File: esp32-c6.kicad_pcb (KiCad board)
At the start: 2 copper layers, 97.1 x 66.5 mm, 80 parts, among them J1 USB_C_Receptacle_USB2.0_14P, J2 USB_C_Receptacle_USB2.0_14P, J3 54-00166, J4 Conn_01x08_Socket, J5 Conn_01x06_Socket, J6 Conn_01x04, J7 Conn_01x10_Socket, J8 Conn_01x08_Socket, J9 Conn_02x03_Counter_Clockwise, Q1 BC847BDW1, SW1 SW_Push, SW2 SW_Push, U1 CP2102N-Axx-xQFN28, U2 MPQ9841GLE-5-AEC1-Z, U3 NCP1117-3.3_SOT223, U4 ESP32-C6-WROOM-1-N8

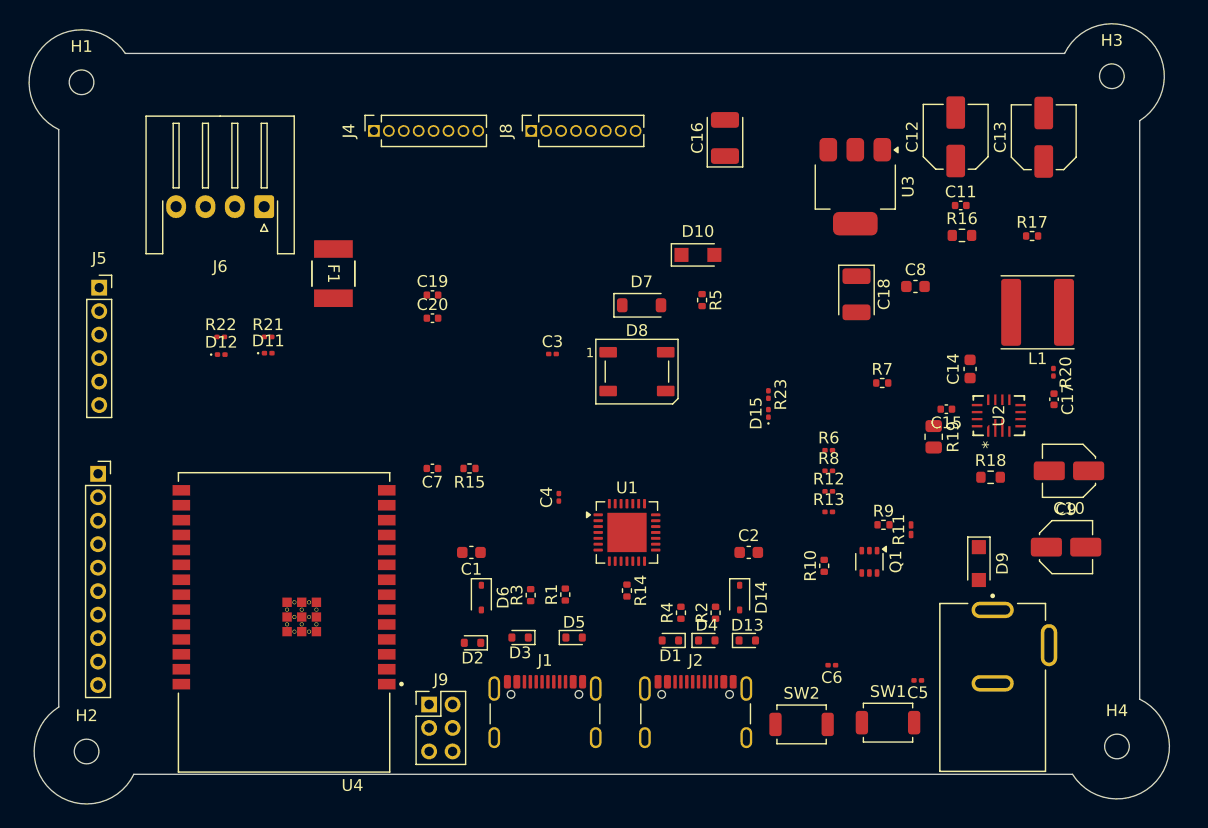
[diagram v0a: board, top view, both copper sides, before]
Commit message: layout + power pin traces
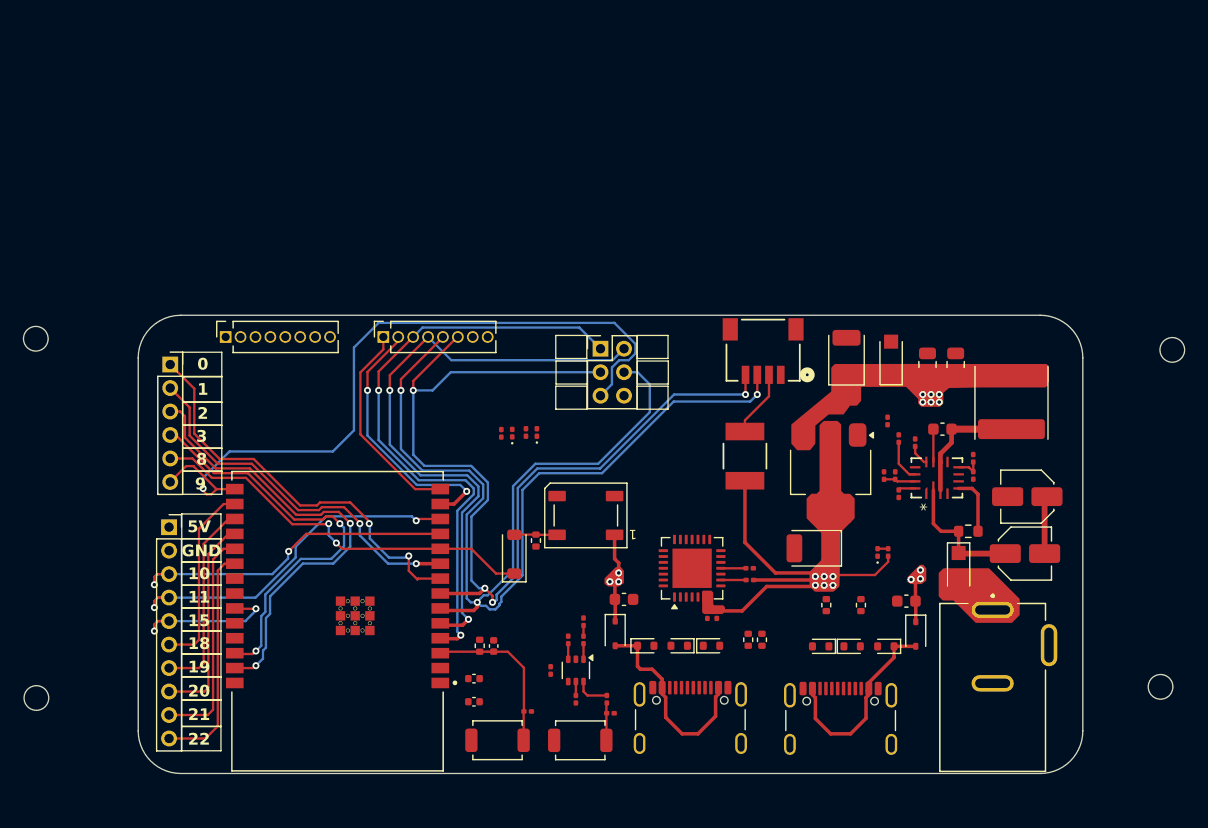
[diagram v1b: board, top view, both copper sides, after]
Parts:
- removed R6: 0, Resistor_SMD:R_0201_0603Metric
- C11, C15, C17: footprint Capacitor_SMD:C_0402_1005Metric -> Capacitor_SMD:C_0201_0603Metric
- C12, C13: footprint Capacitor_SMD:C_Elec_5x5.8 -> Capacitor_SMD:C_0805_2012Metric
- C14: footprint Capacitor_SMD:C_0603_1608Metric -> Capacitor_SMD:C_0201_0603Metric
- J6: footprint Connector_JST:JST_XH_S4B-XH-A-1_1x04_P2.50mm_Horizontal -> uno-esp:CONN_SM04B-SRSS-TB_JST
- R10, R14, R17, R7, R9: footprint Resistor_SMD:R_0402_1005Metric -> Resistor_SMD:R_0201_0603Metric
- R11: footprint Resistor_SMD:R_0201_0603Metric_Pad0.64x0.40mm_HandSolder -> Resistor_SMD:R_0201_0603Metric
- R16: footprint Resistor_SMD:R_0603_1608Metric -> Resistor_SMD:R_0201_0603Metric
- R19: footprint Resistor_SMD:R_0805_2012Metric -> Resistor_SMD:R_0201_0603Metric
- moved J6 44.2 mm to (222.2, 146.5), turned to 0 degrees
- moved F1 38.3 mm to (220.7, 155.6)
- moved J9 33.6 mm to (208.3, 146.4)
- moved C19 32.9 mm to (197.6, 174.5)
- moved C20 32.9 mm to (197.6, 176.5)
- moved R11 29.0 mm to (206.9, 169.7), turned to -90 degrees
- moved R12 27.9 mm to (206.2, 176.3), turned to -90 degrees
- moved D12 27.7 mm to (202.9, 153.5), turned to 90 degrees
- moved R9 27.4 mm to (206.9, 171.2), turned to 90 degrees
- moved R22 27.2 mm to (202.0, 153.5), turned to 90 degrees
- moved R8 27.1 mm to (208.9, 176.3), turned to 90 degrees
- moved Q1 26.7 mm to (206.2, 173.8)
- moved C5 26.3 mm to (209.2, 177.4)
- moved SW1 26.3 mm to (206.6, 179.8)
- moved C3 26.2 mm to (218.2, 169.1), turned to -90 degrees
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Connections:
- C6 pad 2: /EN -> EN
- C7 pad 1: /EN -> EN
- D7 pad 1: /GPIO8 -> IO8
- D8 pad 4: Net-(D8-DIN) -> Net-(D7-A)
- J4 pad 3: /esp32-c6 Pinout/EN -> EN
- J5 pad 5: /esp32-c6 Pinout/IO8 -> IO8
- J9 pad 3: /esp32-c6 Pinout/IO7_TD0 -> /esp32-c6 Pinout/IO7_SCL
- J9 pad 4: /esp32-c6 Pinout/IO6_TCK -> /esp32-c6 Pinout/IO6_SDA
- R15 pad 2: /EN -> EN
- SW2 pad 2: /EN -> EN
- U1 pad 4: /D+_A -> /DA_P
- U1 pad 5: /D-_A -> /DA_N
- U4 pad 10: /esp32-c6 Pinout/IO8 -> IO8
- U4 pad 3: /esp32-c6 Pinout/EN -> EN
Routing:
- net /esp32-c6 Pinout/IO6_SDA: track 0.00 -> 103.0 mm, vias 0 -> 3
- net /esp32-c6 Pinout/IO7_SCL: track 0.00 -> 86.5 mm, vias 0 -> 4
- net /esp32-c6 Pinout/IO9_BOOT: track 0.00 -> 62.7 mm, vias 0 -> 1
- net /esp32-c6 Pinout/IO5_TDI: track 0.00 -> 52.3 mm, vias 0 -> 2
- net /esp32-c6 Pinout/IO4_TMS: track 0.00 -> 52.1 mm, vias 0 -> 2
- net /esp32-c6 Pinout/IO2: track 0.00 -> 39.5 mm, vias 0 -> 2
- net /esp32-c6 Pinout/IO3: track 0.00 -> 35.3 mm, vias 0 -> 2
- net +3.3V: track 0.00 -> 35.1 mm, vias 0 -> 6
- net /esp32-c6 Pinout/IO0: track 0.00 -> 34.7 mm, vias 0 -> 2
- net IO8: track 0.00 -> 34.0 mm, vias 0 -> 2
- net /esp32-c6 Pinout/IO1: track 0.00 -> 31.4 mm, vias 0 -> 2
- net /esp32-c6 Pinout/IO11: track 0.00 -> 30.8 mm, vias 0 -> 2
- net /esp32-c6 Pinout/IO10: track 0.00 -> 28.8 mm, vias 0 -> 2
- net /esp32-c6 Pinout/IO12_DB_N: track 0.00 -> 22.6 mm, vias 0 -> 2
- net /esp32-c6 Pinout/IO22: track 0.00 -> 19.5 mm
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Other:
- board size 97.1 x 66.5 mm -> 80.5 x 39 mm
- copper layers 2 -> 4
- board text added: "0"
- board text added: "1"
- board text added: "10"
- board text added: "11"
- board text added: "15"
- board text added: "18"
- board text added: "19"
- board text added: "2"
- board text added: "20"
- board text added: "21"
- board text added: "22"
- board text added: "3"
- board text added: "5V"
- board text added: "8"
- board text added: "9"
- board text added: "GND"

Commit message: final tracing + pcb layers + colors
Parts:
- removed H1, H2, H3, H4: MountingHole, MountingHole:MountingHole_2.1mm
- removed J9: Conn_02x03_Counter_Clockwise, Connector_PinHeader_2.00mm:PinHeader_2x03_P2.00mm_Vertical
- added R6: 0, Resistor_SMD:R_0402_1005Metric_Pad0.72x0.64mm_HandSolder, F.Cu at (181.8, 152.7)
- J4: footprint Connector_PinSocket_1.27mm:PinSocket_1x08_P1.27mm_Vertical -> Connector_PinSocket_2.00mm:PinSocket_1x08_P2.00mm_Vertical
- J8: value Conn_01x08_Socket -> Conn_01x06_Socket; footprint Connector_PinSocket_1.27mm:PinSocket_1x08_P1.27mm_Vertical -> Connector_PinSocket_2.00mm:PinSocket_1x06_P2.00mm_Vertical
- moved J6 28.0 mm to (194.2, 146.5)
- moved J4 24.7 mm to (201.1, 145.4)
- moved F1 23.9 mm to (196.8, 153.4), turned to 0 degrees
- moved D11 20.8 mm to (180.1, 152.4), turned to -90 degrees
- moved R21 20.3 mm to (179.8, 150.9), turned to 180 degrees
- moved D12 19.5 mm to (183.5, 152.4), turned to -90 degrees
- moved R22 19.0 mm to (183.2, 151.0), turned to 180 degrees
- moved D10 13.8 mm to (219.3, 146.1), turned to 180 degrees
- moved J8 12.6 mm to (177.2, 145.4)
- moved D1 2.68 mm to (229.8, 171.8), turned to 0 degrees
- moved D4 2.68 mm to (227.1, 171.8), turned to 180 degrees
- moved C20 2.43 mm to (197.1, 174.1), turned to -90 degrees
- moved C19 0.66 mm to (198.1, 174.1), turned to -90 degrees
- turned D7 to -90 degrees
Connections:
- C9 pad 1: /Barrel Jack/VIN -> VIN
- D1 pad 1: /IO13_DB_P -> DB_P
- D10 pad 1: +5V -> VIN
- D10 pad 2: VBUS -> Net-(D10-A)
- D4 pad 1: /IO12_DB_N -> DB_N
- D9 pad 1: /Barrel Jack/VIN -> VIN
- D9 pad 2: V_IN -> VIN
- J2 pad A6: /IO13_DB_P -> DB_P
- J2 pad A7: /IO12_DB_N -> DB_N
- J2 pad B6: /IO13_DB_P -> DB_P
- J2 pad B7: /IO12_DB_N -> DB_N
- J3 pad A: V_IN -> VIN
- J4 pad 8: VIN -> Net-(D10-A)
- J8 pad 1: /esp32-c6 Pinout/IO13_DB_P -> /esp32-c6 Pinout/IO4_TMS
- J8 pad 2: /esp32-c6 Pinout/IO12_DB_N -> /esp32-c6 Pinout/IO5_TDI
- J8 pad 3: /esp32-c6 Pinout/IO4_TMS -> /esp32-c6 Pinout/IO6_SDA
- J8 pad 4: /esp32-c6 Pinout/IO5_TDI -> /esp32-c6 Pinout/IO7_SCL
- J8 pad 5: /esp32-c6 Pinout/IO6_SDA -> /esp32-c6 Pinout/UART_TX
- J8 pad 6: /esp32-c6 Pinout/IO7_SCL -> /esp32-c6 Pinout/UART_RX
- R18 pad 1: /Barrel Jack/VIN -> VIN
- U2 pad 2: /Barrel Jack/VIN -> VIN
- U4 pad 13: /esp32-c6 Pinout/IO12_DB_N -> DB_N
- U4 pad 14: /esp32-c6 Pinout/IO13_DB_P -> DB_P
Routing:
- net +5V: track 11.4 -> 134.3 mm, vias 12 -> 14
- net +3.3V: track 35.1 -> 144.4 mm, vias 6 -> 9
- net /esp32-c6 Pinout/IO9_BOOT: track 62.7 -> 6.87 mm, vias 1 -> 0
- net VIN: track 0.00 -> 50.3 mm, vias 0 -> 4
- net DB_P: track 0.00 -> 49.8 mm, vias 0 -> 2
- net DB_N: track 0.00 -> 47.5 mm, vias 0 -> 2
- net EN: track 13.9 -> 48.8 mm, vias 0 -> 1
- net /esp32-c6 Pinout/UART_RX: track 0.00 -> 32.2 mm, vias 0 -> 2
- net /esp32-c6 Pinout/UART_TX: track 0.00 -> 31.8 mm, vias 0 -> 2
- net /esp32-c6 Pinout/IO6_SDA: track 103.0 -> 72.9 mm, vias 3 -> 1
- net /esp32-c6 Pinout/IO12_DB_N: track 22.6 -> 0.00 mm, vias 2 -> 0
- net /esp32-c6 Pinout/IO13_DB_P: track 17.8 -> 0.00 mm
- net /esp32-c6 Pinout/IO7_SCL: track 86.5 -> 69.5 mm, vias 4 -> 1
- net /DA_N: track 0.00 -> 12.9 mm, vias 0 -> 1
- net Net-(J2-CC2): track 0.00 -> 12.6 mm, vias 0 -> 2
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- added copper zone on B.Cu, net GND
- added copper zone on F.Cu, net GND
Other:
- board size 80.5 x 39 mm -> 78.5 x 39 mm
- copper layers 4 -> 2
- board text added: "3.3"
- board text added: "4"
- board text added: "5"
- board text added: "6"
- board text added: "7"
- board text added: "EN"
- board text added: "RX"
- board text added: "TX"
- board text added: "VIN"

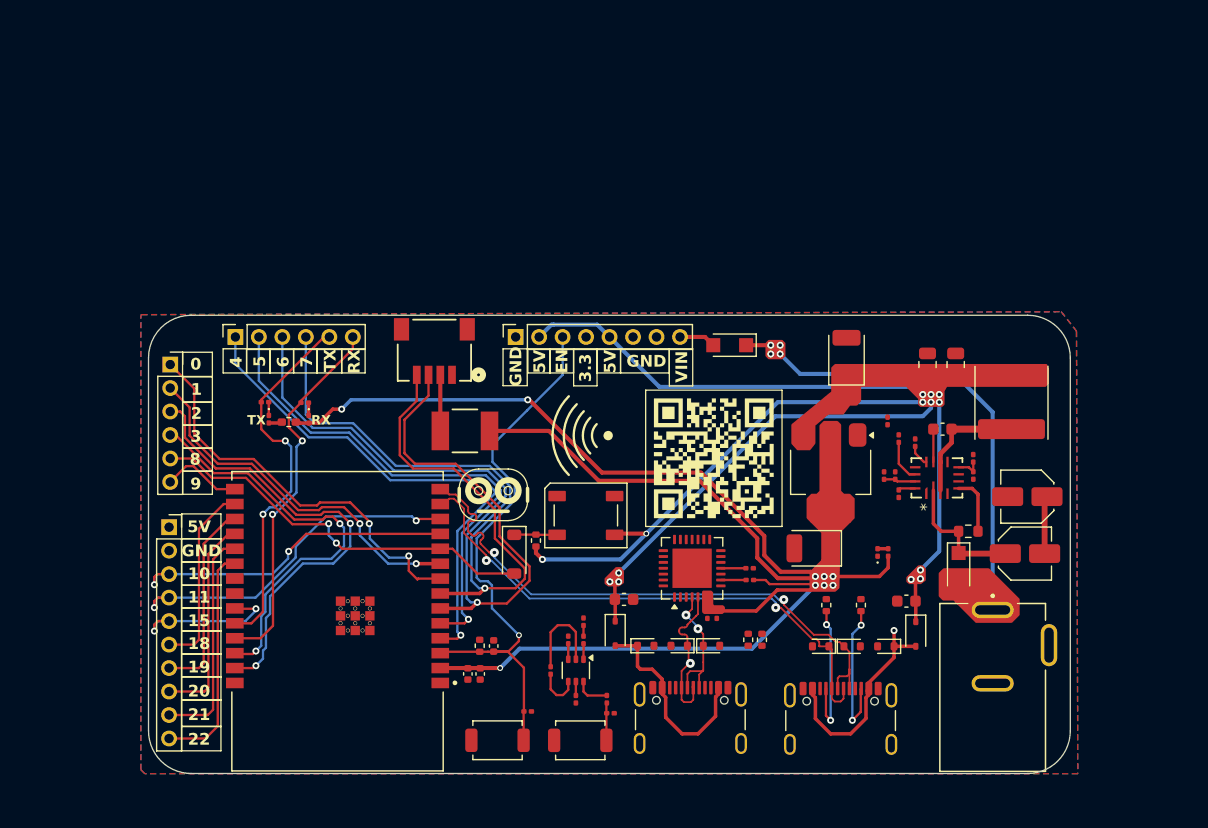
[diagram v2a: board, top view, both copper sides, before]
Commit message: minor silkscreen changes + readme file
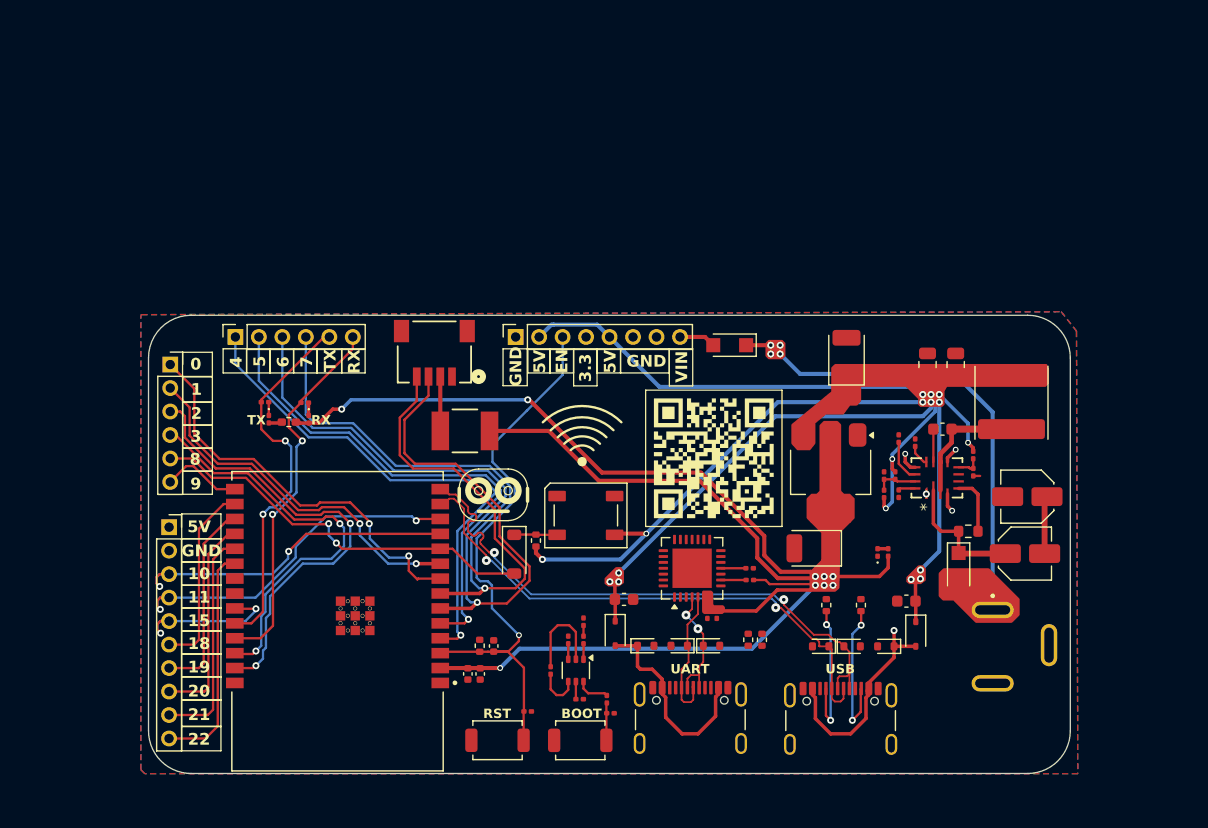
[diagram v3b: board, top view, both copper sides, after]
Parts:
- moved C11 6.22 mm to (232.5, 158.8), turned to 90 degrees
- moved R12 0.32 mm to (206.6, 176.2), turned to 0 degrees
- moved C17 0.28 mm to (240.1, 156.9)
- moved R20 0.28 mm to (240.1, 155.5)
- moved J6 0.15 mm to (194.2, 146.7)
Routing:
- net +5V: track 134.3 -> 153.4 mm, vias 14 -> 17
- net GND: track 0.03 -> 5.31 mm, vias 0 -> 4
- net /DA_N: track 12.9 -> 11.8 mm, vias 1 -> 0
- net /Barrel Jack/VOUT: track 2.72 -> 3.65 mm
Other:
- board text added: "BOOT"
- board text added: "RST"
- board text added: "UART"
- board text added: "USB"
